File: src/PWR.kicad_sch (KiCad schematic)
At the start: 57 parts, among them J1 USB_C_Receptacle_USB2.0_16P, Q11 SI2308A, Q12 SI2308A, Q13 SI2308A, Q4 SI2319A, Q5 SI2319A, U11 TPS7B69xx, U14 TPS54302DDCR, U4 TPS54302DDCR

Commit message: pcb layout continued
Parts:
- C3, C42, C43, C5: symbol Capacitor:CL32A476KOJNNNE -> Capacitor:CS3225X7R476K160NRL; Dielectric X5R -> X7R; LCSC Part C2932477 -> C5440143; Manufacturer 1 Samsung Electro-Mechanics -> Samwha Capacitor; Manufacturer Part Number 1 CL32A476KOJNNNE -> CS3225X7R476K160NRL; Price @1 USD 0.2665 -> 0.3615; Price @100 USD 0.1851 -> 0.2960; Price @Bulk USD 0.1693 -> 0.2339; Price Updated 2026-06-14 -> 2026-07-16; Supplier Part Number 1 C2932477 -> C5440143
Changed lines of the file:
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@@
 	)
 	(symbol
-		(lib_id "Capacitor:CL32A476KOJNNNE")
+		(lib_id "Capacitor:CS3225X7R476K160NRL")
 		(at 251.46 77.47 0)
 		(unit 1)
@@
 			)
 		)
-		(property "Datasheet" "https://datasheet.lcsc.com/datasheet/pdf/3cd38c41b24c01cdc3c62ae025f7fc43.pdf?productCode=C2932477"
+		(property "Datasheet" "https://datasheet.lcsc.com/lcsc/2411201415_SAMWHA-CS3225X7R476K160NRL_C5440143.pdf"
 			(at 251.46 77.47 0)
 			(hide yes)
@@
 			)
 		)
-		(property "Description" "47uF 16V X5R 10% 1210"
+		(property "Description" "47uF 16V X7R 10% 1210"
 			(at 251.46 77.47 0)
 			(hide yes)
@@
 			)
 		)
-		(property "Dielectric" "X5R"
+		(property "Dielectric" "X7R"
 			(at 250.19 78.994 0)
 			(show_name no)
@@
 			)
 		)
-		(property "Manufacturer 1" "Samsung Electro-Mechanics"
+		(property "Manufacturer 1" "Samwha Capacitor"
 			(at 251.46 77.47 0)
 			(hide yes)
@@
 			)
 		)
-		(property "Manufacturer Part Number 1" "CL32A476KOJNNNE"
+		(property "Manufacturer Part Number 1" "CS3225X7R476K160NRL"
 			(at 251.46 77.47 0)
 			(hide yes)
@@
 			)
 		)
-		(property "Supplier Part Number 1" "C2932477"
+		(property "Supplier Part Number 1" "C5440143"
 			(at 251.46 77.47 0)
 			(hide yes)
@@
 			)
 		)
-		(property "LCSC Part" "C2932477"
+		(property "LCSC Part" "C5440143"
 			(at 251.46 77.47 0)
 			(hide yes)
@@
 			)
 		)
-		(property "Price @1 USD" "0.2665"
+		(property "Price @1 USD" "0.3615"
 			(at 251.46 77.47 0)
 			(hide yes)
@@
 			)
 		)
-		(property "Price @100 USD" "0.1851"
+		(property "Price @100 USD" "0.2960"
 			(at 251.46 77.47 0)
 			(hide yes)
@@
 			)
 		)
-		(property "Price @Bulk USD" "0.1693"
+		(property "Price @Bulk USD" "0.2339"
 			(at 251.46 77.47 0)
 			(hide yes)
@@
 			)
 		)
-		(property "Price Updated" "2026-06-14"
+		(property "Price Updated" "2026-07-16"
 			(at 251.46 77.47 0)
 			(hide yes)
@@
 	)
 	(symbol
-		(lib_id "Capacitor:CL32A476KOJNNNE")
+		(lib_id "Capacitor:CS3225X7R476K160NRL")
 		(at 259.08 41.91 0)
 		(unit 1)
@@
 			)
 		)
-		(property "Datasheet" "https://datasheet.lcsc.com/datasheet/pdf/3cd38c41b24c01cdc3c62ae025f7fc43.pdf?productCode=C2932477"
+		(property "Datasheet" "https://datasheet.lcsc.com/lcsc/2411201415_SAMWHA-CS3225X7R476K160NRL_C5440143.pdf"
 			(at 259.08 41.91 0)
 			(hide yes)
@@
 			)
 		)
-		(property "Description" "47uF 16V X5R 10% 1210"
+		(property "Description" "47uF 16V X7R 10% 1210"
 			(at 259.08 41.91 0)
 			(hide yes)
@@
 			)
 		)
-		(property "Dielectric" "X5R"
+		(property "Dielectric" "X7R"
 			(at 257.81 43.434 0)
 			(show_name no)
@@
 			)
 		)
-		(property "Manufacturer 1" "Samsung Electro-Mechanics"
+		(property "Manufacturer 1" "Samwha Capacitor"
 			(at 259.08 41.91 0)
 			(hide yes)
@@
 			)
 		)
-		(property "Manufacturer Part Number 1" "CL32A476KOJNNNE"
+		(property "Manufacturer Part Number 1" "CS3225X7R476K160NRL"
 			(at 259.08 41.91 0)
 			(hide yes)
@@
 			)
 		)
-		(property "Supplier Part Number 1" "C2932477"
+		(property "Supplier Part Number 1" "C5440143"
 			(at 259.08 41.91 0)
 			(hide yes)
@@
 			)
 		)
-		(property "LCSC Part" "C2932477"
+		(property "LCSC Part" "C5440143"
 			(at 259.08 41.91 0)
 			(hide yes)
@@
 			)
 		)
-		(property "Price @1 USD" "0.2665"
+		(property "Price @1 USD" "0.3615"
 			(at 259.08 41.91 0)
 			(hide yes)
@@
 			)
 		)
-		(property "Price @100 USD" "0.1851"
+		(property "Price @100 USD" "0.2960"
 			(at 259.08 41.91 0)
 			(hide yes)
@@
 			)
 		)
-		(property "Price @Bulk USD" "0.1693"
+		(property "Price @Bulk USD" "0.2339"
 			(at 259.08 41.91 0)
 			(hide yes)
@@
 			)
 		)
-		(property "Price Updated" "2026-06-14"
+		(property "Price Updated" "2026-07-16"
 			(at 259.08 41.91 0)
 			(hide yes)
@@
 	)
 	(symbol
-		(lib_id "Capacitor:CL32A476KOJNNNE")
+		(lib_id "Capacitor:CS3225X7R476K160NRL")
 		(at 259.08 77.47 0)
 		(unit 1)
@@
 			)
 		)
-		(property "Datasheet" "https://datasheet.lcsc.com/datasheet/pdf/3cd38c41b24c01cdc3c62ae025f7fc43.pdf?productCode=C2932477"
+		(property "Datasheet" "https://datasheet.lcsc.com/lcsc/2411201415_SAMWHA-CS3225X7R476K160NRL_C5440143.pdf"
 			(at 259.08 77.47 0)
 			(hide yes)
@@
 			)
 		)
-		(property "Description" "47uF 16V X5R 10% 1210"
+		(property "Description" "47uF 16V X7R 10% 1210"
 			(at 259.08 77.47 0)
 			(hide yes)
@@
 			)
 		)
-		(property "Dielectric" "X5R"
+		(property "Dielectric" "X7R"
 			(at 257.81 78.994 0)
 			(show_name no)
@@
 			)
 		)
-		(property "Manufacturer 1" "Samsung Electro-Mechanics"
+		(property "Manufacturer 1" "Samwha Capacitor"
 			(at 259.08 77.47 0)
 			(hide yes)
@@
 			)
 		)
-		(property "Manufacturer Part Number 1" "CL32A476KOJNNNE"
+		(property "Manufacturer Part Number 1" "CS3225X7R476K160NRL"
 			(at 259.08 77.47 0)
 			(hide yes)
@@
 			)
 		)
-		(property "Supplier Part Number 1" "C2932477"
+		(property "Supplier Part Number 1" "C5440143"
 			(at 259.08 77.47 0)
 			(hide yes)
@@
 			)
 		)
-		(property "LCSC Part" "C2932477"
+		(property "LCSC Part" "C5440143"
 			(at 259.08 77.47 0)
 			(hide yes)
@@
 			)
 		)
-		(property "Price @1 USD" "0.2665"
+		(property "Price @1 USD" "0.3615"
 			(at 259.08 77.47 0)
 			(hide yes)
@@
 			)
 		)
-		(property "Price @100 USD" "0.1851"
+		(property "Price @100 USD" "0.2960"
 			(at 259.08 77.47 0)
 			(hide yes)
@@
 			)
 		)
-		(property "Price @Bulk USD" "0.1693"
+		(property "Price @Bulk USD" "0.2339"
 			(at 259.08 77.47 0)
 			(hide yes)
@@
 			)
 		)
-		(property "Price Updated" "2026-06-14"
+		(property "Price Updated" "2026-07-16"
 			(at 259.08 77.47 0)
 			(hide yes)
@@
 	)
 	(symbol
-		(lib_id "Capacitor:CL32A476KOJNNNE")
+		(lib_id "Capacitor:CS3225X7R476K160NRL")
 		(at 251.46 41.91 0)
 		(unit 1)
@@
 			)
 		)
-		(property "Datasheet" "https://datasheet.lcsc.com/datasheet/pdf/3cd38c41b24c01cdc3c62ae025f7fc43.pdf?productCode=C2932477"
+		(property "Datasheet" "https://datasheet.lcsc.com/lcsc/2411201415_SAMWHA-CS3225X7R476K160NRL_C5440143.pdf"
 			(at 251.46 41.91 0)
 			(hide yes)
@@
 			)
 		)
-		(property "Description" "47uF 16V X5R 10% 1210"
+		(property "Description" "47uF 16V X7R 10% 1210"
 			(at 251.46 41.91 0)
 			(hide yes)
@@
 			)
 		)
-		(property "Dielectric" "X5R"
+		(property "Dielectric" "X7R"
 			(at 250.19 43.434 0)
 			(show_name no)
@@
 			)
 		)
-		(property "Manufacturer 1" "Samsung Electro-Mechanics"
+		(property "Manufacturer 1" "Samwha Capacitor"
 			(at 251.46 41.91 0)
 			(hide yes)
@@
 			)
 		)
-		(property "Manufacturer Part Number 1" "CL32A476KOJNNNE"
+		(property "Manufacturer Part Number 1" "CS3225X7R476K160NRL"
 			(at 251.46 41.91 0)
 			(hide yes)
@@
 			)
 		)
-		(property "Supplier Part Number 1" "C2932477"
+		(property "Supplier Part Number 1" "C5440143"
 			(at 251.46 41.91 0)
 			(hide yes)
@@
 			)
 		)
-		(property "LCSC Part" "C2932477"
+		(property "LCSC Part" "C5440143"
 			(at 251.46 41.91 0)
 			(hide yes)
@@
 			)
 		)
-		(property "Price @1 USD" "0.2665"
+		(property "Price @1 USD" "0.3615"
 			(at 251.46 41.91 0)
 			(hide yes)
@@
 			)
 		)
-		(property "Price @100 USD" "0.1851"
+		(property "Price @100 USD" "0.2960"
 			(at 251.46 41.91 0)
 			(hide yes)
@@
 			)
 		)
-		(property "Price @Bulk USD" "0.1693"
+		(property "Price @Bulk USD" "0.2339"
 			(at 251.46 41.91 0)
 			(hide yes)
@@
 			)
 		)
-		(property "Price Updated" "2026-06-14"
+		(property "Price Updated" "2026-07-16"
 			(at 251.46 41.91 0)
 			(hide yes)

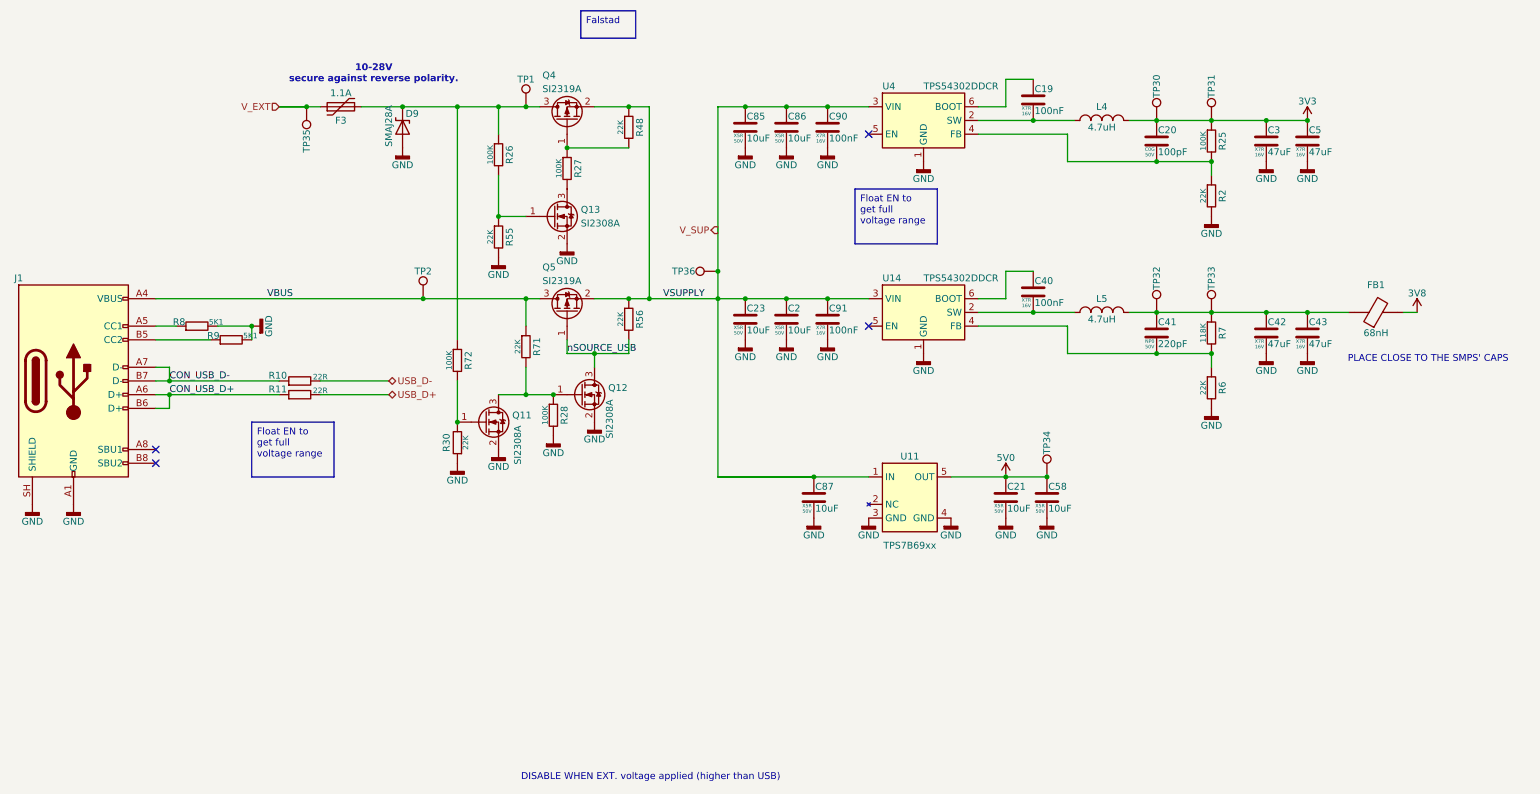
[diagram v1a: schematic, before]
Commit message: layout + lib swap to http library. changed up the 10u and 47u caps for cheaper alternative
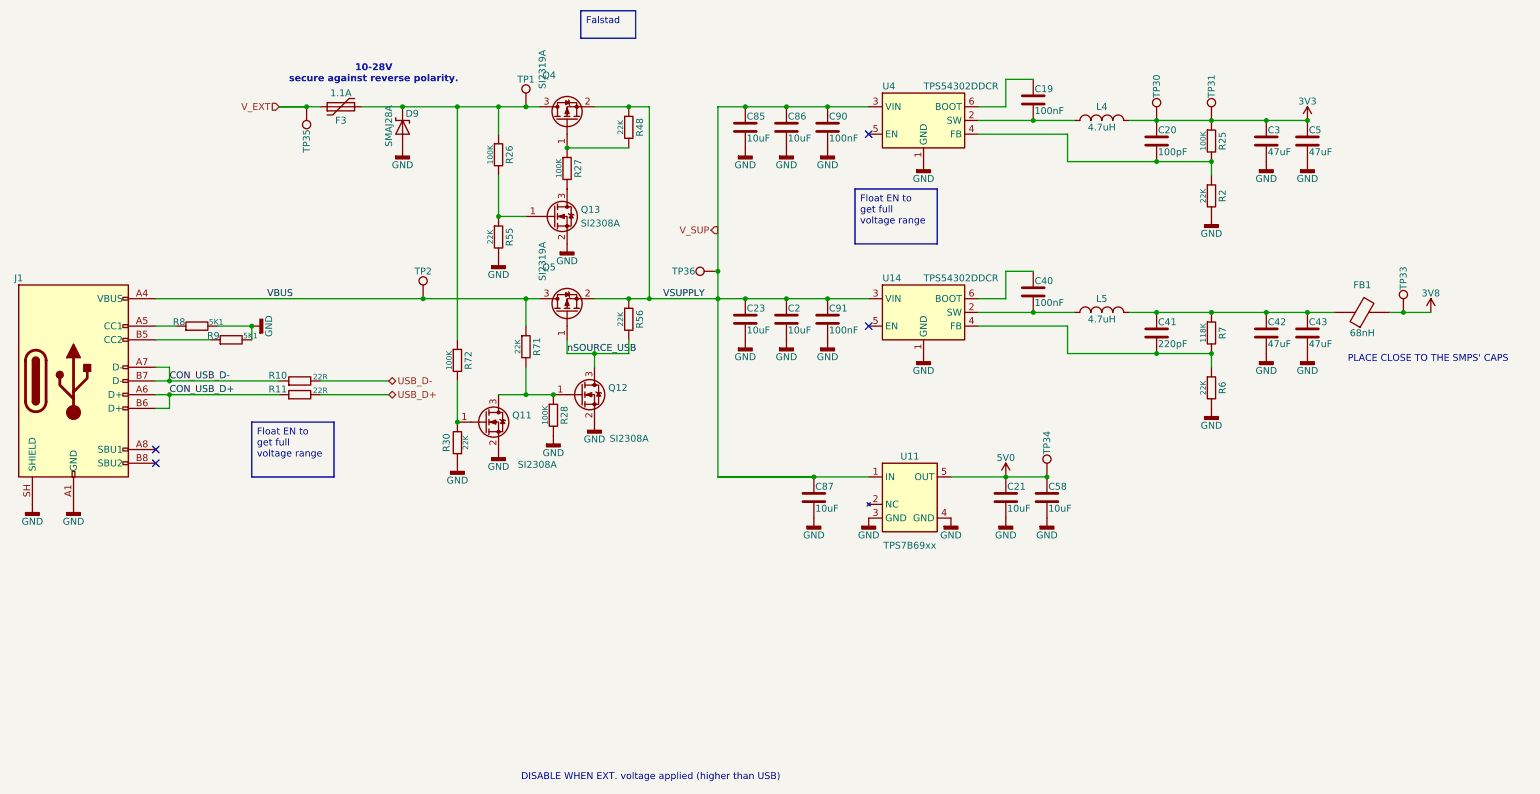
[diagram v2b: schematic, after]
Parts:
- removed TP32: TestPoint, 7Sigma:TestPoint_Pad_D1.5mm, symbol TestPoints:TestPoint_Pad_D1.5mm
- C19, C40, C90, C91: footprint 7Sigma:C_0402_1005Metric -> PCM_7Sigma:C_0402_1005Metric; symbol Capacitor:CL05B104KO5NNNC -> 7Sigma:CL05B104KO5NNNC; Price @1 USD 0.0015 -> (none); Price @100 USD 0.0015 -> (none); Price @Bulk USD 0.0012 -> (none); Price Bulk Qty 1000 -> (none); Price Source LCSC -> (none); Price Updated 2026-05-14 -> (none)
- C2, C21, C23, C58, C85, C86, C87: footprint 7Sigma:C_0805_2012Metric -> PCM_7Sigma:C_0805_2012Metric; symbol Capacitor:GRM21BR61H106KE43L -> 7Sigma:GRM21BR61H106KE43L; Manufacturer 1 muRata -> Murata; Price @1 USD 0.0690 -> (none); Price @100 USD 0.0561 -> (none); Price @Bulk USD 0.0494 -> (none); Price Bulk Qty 300 -> (none); Price Source LCSC -> (none); Price Updated 2026-05-14 -> (none)
- C20: footprint 7Sigma:C_0402_1005Metric -> PCM_7Sigma:C_0402_1005Metric; symbol Capacitor:0402CG101J500NT -> 7Sigma:0402CG101J500NT; Manufacturer 1 FH -> FH (Guangdong Fenghua Advanced Tech); Price @1 USD 0.0020 -> (none); Price @100 USD 0.0020 -> (none); Price @Bulk USD 0.0017 -> (none); Price Bulk Qty 1000 -> (none); Price Source LCSC -> (none); Price Updated 2026-06-14 -> (none)
- C3, C42, C43, C5: footprint 7Sigma:C_1210_3225Metric -> PCM_7Sigma:C_1210_3225Metric; symbol Capacitor:CS3225X7R476K160NRL -> 7Sigma:CS3225X7R476K160NRL; Price @1 USD 0.3615 -> (none); Price @100 USD 0.2960 -> (none); Price @Bulk USD 0.2339 -> (none); Price Bulk Qty 1000 -> (none); Price Source LCSC -> (none); Price Updated 2026-07-16 -> (none)
- C41: footprint 7Sigma:C_0402_1005Metric -> PCM_7Sigma:C_0402_1005Metric; symbol Capacitor:CC0402JRNPO9BN221 -> 7Sigma:CC0402JRNPO9BN221; Manufacturer 1 YAGEO -> Yageo; Price @1 USD 0.0029 -> (none); Price @100 USD 0.0029 -> (none); Price @Bulk USD 0.0022 -> (none); Price Bulk Qty 1000 -> (none); Price Source LCSC -> (none); Price Updated 2026-05-14 -> (none)
- D9: footprint 7Sigma:D_SMA -> PCM_7Sigma:D_SMA; symbol Diodes:SMAJ28A -> 7Sigma:SMAJ28A; Clamping Voltage (none) -> 45.4V; Footprint_Name (none) -> SMA; Price @1 USD 0.1321 -> (none); Price @100 USD 0.1099 -> (none); Price @Bulk USD 0.0904 -> (none); Price Bulk Qty 500 -> (none); Price Source LCSC -> (none); Price Updated 2026-07-17 -> (none)
- F3: footprint 7Sigma:Fuse_1206_3216Metric -> PCM_7Sigma:Fuse_1206_3216Metric; symbol Circuit_Protection:BSMD1206-110-30V -> 7Sigma:BSMD1206-110-30V; Price @1 USD 0.1468 -> (none); Price @100 USD 0.1135 -> (none); Price @Bulk USD 0.0844 -> (none); Price Bulk Qty 500 -> (none); Price Source LCSC -> (none); Price Updated 2026-07-17 -> (none)
- FB1: footprint 7Sigma:L_0603_1608Metric -> PCM_7Sigma:L_0603_1608Metric; symbol Inductors:BLM18EG101TN1D -> 7Sigma:BLM18EG101TN1D; Manufacturer 1 muRata -> Murata Electronics; Price @1 USD 0.0538 -> (none); Price @100 USD 0.0538 -> (none); Price @Bulk USD 0.0408 -> (none); Price Bulk Qty 600 -> (none); Price Source LCSC -> (none); Price Updated 2026-05-14 -> (none)
- J1: footprint 7Sigma:USB-3.1-SMD_U262-161N-4BVC11 -> PCM_7Sigma:USB-3.1-SMD_U262-161N-4BVC11; symbol Connectors:U262-161N-4BVC11 -> 7Sigma:U262-161N-4BVC11; Price @1 USD 0.3864 -> (none); Price @100 USD 0.3059 -> (none); Price @Bulk USD 0.2316 -> (none); Price Bulk Qty 1000 -> (none); Price Source LCSC -> (none); Price Updated 2026-05-14 -> (none)
- L4, L5: footprint 7Sigma:L_Changjiang_FTC404030S -> PCM_7Sigma:L_Changjiang_FTC404030S; symbol Inductors:FTC404030S4R7MGCA -> 7Sigma:FTC404030S4R7MGCA; Manufacturer 1 cjiang -> Changjiang Microelectronics Technology; Price @1 USD 0.2442 -> (none); Price @100 USD 0.1909 -> (none); Price @Bulk USD 0.1397 -> (none); Price Bulk Qty 500 -> (none); Price Source LCSC -> (none); Price Updated 2026-05-14 -> (none)
- Q11, Q12, Q13: footprint 7Sigma:SOT-23-3 -> PCM_7Sigma:SOT-23-3; symbol Transistors:SI2308A -> 7Sigma:SI2308A; Manufacturer 1 UMW -> UMW (Youtai Semiconductor Co., Ltd.); Price @1 USD 0.0364 -> (none); Price @100 USD 0.0284 -> (none); Price @Bulk USD 0.0242 -> (none); Price Bulk Qty 300 -> (none); Price Source LCSC -> (none); Price Updated 2026-05-14 -> (none)
- Q4, Q5: footprint 7Sigma:SOT-23-3 -> PCM_7Sigma:SOT-23-3; symbol Transistors:SI2319A -> 7Sigma:SI2319A; Manufacturer 1 UMW -> UMW (Youtai Semiconductor Co., Ltd.); Price @1 USD 0.0585 -> (none); Price @100 USD 0.0455 -> (none); Price @Bulk USD 0.0390 -> (none); Price Bulk Qty 300 -> (none); Price Source LCSC -> (none); Price Updated 2026-07-16 -> (none)
- R10, R11: footprint 7Sigma:R_0402_1005Metric -> PCM_7Sigma:R_0402_1005Metric; symbol Resistor:0402WGF220JTCE -> 7Sigma:0402WGF220JTCE; Manufacturer 1 Uni-Royal -> UNI-ROYAL(Uniroyal Elec); Price @1 USD 0.0007 -> (none); Price @100 USD 0.0007 -> (none); Price @Bulk USD 0.0006 -> (none); Price Bulk Qty 1000 -> (none); Price Source LCSC -> (none); Price Updated 2026-05-14 -> (none)
- R2, R30, R48, R55, R56, R6, R71: footprint 7Sigma:R_0402_1005Metric -> PCM_7Sigma:R_0402_1005Metric; symbol Resistor:0402WGF2202TCE -> 7Sigma:0402WGF2202TCE; Manufacturer 1 Uni-Royal -> UNI-ROYAL(Uniroyal Elec); Price @1 USD 0.0010 -> (none); Price @100 USD 0.0010 -> (none); Price @Bulk USD 0.0008 -> (none); Price Bulk Qty 1000 -> (none); Price Source LCSC -> (none); Price Updated 2026-05-14 -> (none)
- R25, R26, R27, R28, R72: footprint 7Sigma:R_0402_1005Metric -> PCM_7Sigma:R_0402_1005Metric; symbol Resistor:0402WGF1003TCE -> 7Sigma:0402WGF1003TCE; Manufacturer 1 Uni-Royal -> UNI-ROYAL(Uniroyal Elec); Price @1 USD 0.0009 -> (none); Price @100 USD 0.0009 -> (none); Price @Bulk USD 0.0007 -> (none); Price Bulk Qty 1000 -> (none); Price Source LCSC -> (none); Price Updated 2026-05-14 -> (none)
- R7: footprint 7Sigma:R_0402_1005Metric -> PCM_7Sigma:R_0402_1005Metric; symbol Resistor:0402WGF1183TCE -> 7Sigma:0402WGF1183TCE; Manufacturer 1 Uni-Royal -> UNI-ROYAL(Uniroyal Elec); Price @1 USD 0.0004 -> (none); Price @100 USD 0.0004 -> (none); Price @Bulk USD 0.0004 -> (none); Price Bulk Qty 100 -> (none); Price Source LCSC -> (none); Price Updated 2026-05-14 -> (none)
- R8, R9: footprint 7Sigma:R_0402_1005Metric -> PCM_7Sigma:R_0402_1005Metric; symbol Resistor:0402WGF5101TCE -> 7Sigma:0402WGF5101TCE; Manufacturer 1 Uni-Royal -> UNI-ROYAL(Uniroyal Elec); Price @1 USD 0.0009 -> (none); Price @100 USD 0.0009 -> (none); Price @Bulk USD 0.0007 -> (none); Price Bulk Qty 1000 -> (none); Price Source LCSC -> (none); Price Updated 2026-05-14 -> (none)
- TP1, TP2, TP30, TP31, TP33, TP34, TP35, TP36: footprint 7Sigma:TestPoint_Pad_D1.5mm -> PCM_7Sigma:TestPoint_Pad_D1.5mm; symbol TestPoints:TestPoint_Pad_D1.5mm -> 7Sigma:TestPoint_Pad_D1.5mm
- U11: footprint 7Sigma:SOT-23-5 -> PCM_7Sigma:SOT-23-5; symbol ICs:TPS7B6950QDBVRQ1 -> 7Sigma:TPS7B6950QDBVRQ1; Footprint_Name (none) -> SOT-23-5; Manufacturer 1 TI -> Texas Instruments; Output Current 150 mA -> 150mA; Price @1 USD 0.3638 -> (none); Price @100 USD 0.2913 -> (none); Price @Bulk USD 0.2216 -> (none); Price Bulk Qty 500 -> (none); Price Source LCSC -> (none); Price Updated 2026-07-16 -> (none)
- U14, U4: footprint 7Sigma:SOT-23-6 -> PCM_7Sigma:SOT-23-6; symbol ICs:TPS54302DDCR -> 7Sigma:TPS54302DDCR; Footprint_Name (none) -> SOT-23-6; Input Voltage (none) -> 4.5V~28V; Output Current (none) -> 3A; Output Voltage (none) -> Adj; Price @1 USD 0.2927 -> (none); Price @100 USD 0.2293 -> (none); Price @Bulk USD 0.1707 -> (none); Price Bulk Qty 500 -> (none); Price Source LCSC -> (none); Price Updated 2026-05-14 -> (none); Topology (none) -> Buck
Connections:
- net 3V8: now also TP33.1
- net at C41.1, C42.1, C43.1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: no longer TP33.1
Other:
- moved on the sheet: FB1, TP33
